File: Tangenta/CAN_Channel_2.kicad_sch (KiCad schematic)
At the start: 0 parts

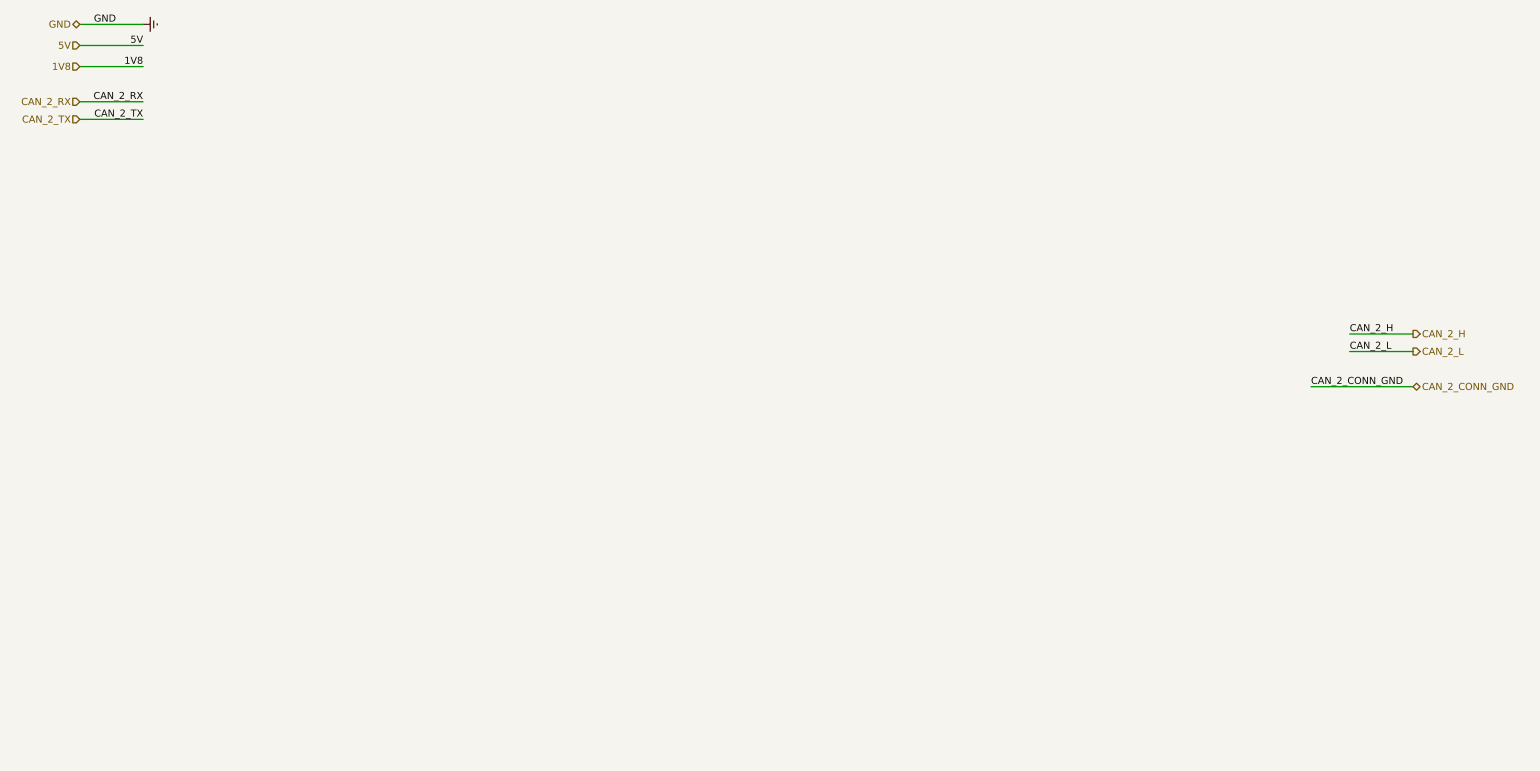
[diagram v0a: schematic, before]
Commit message: CANbus ICs schematic done.
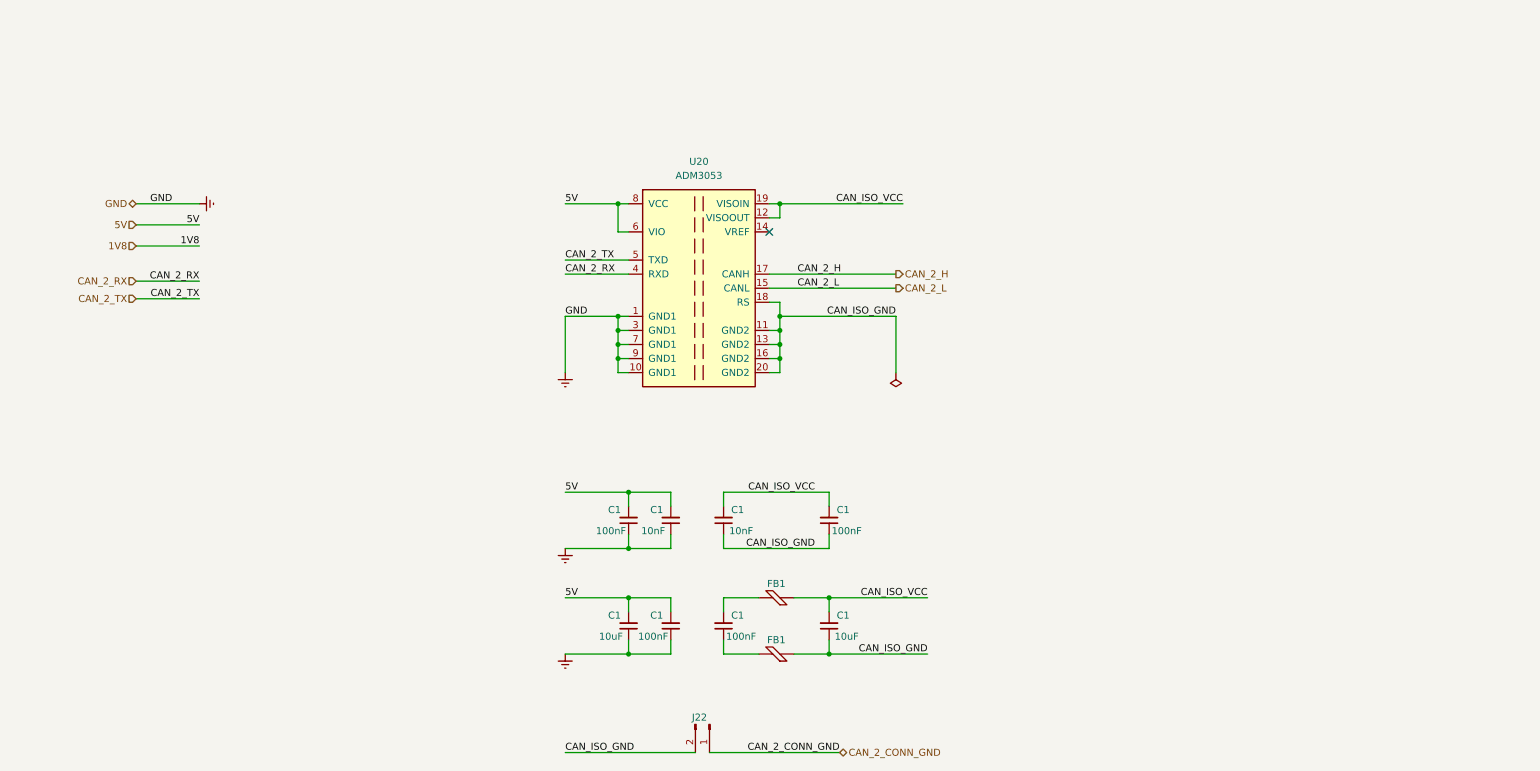
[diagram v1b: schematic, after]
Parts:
- added C1 (x4): 100nF, Capacitor_SMD:C_0402_1005Metric, symbol Device:C_Small
- added C1 (x2): 10uF, Capacitor_SMD:C_0402_1005Metric, symbol Device:C_Small
- added C1 (x2): 10nF, Capacitor_SMD:C_0402_1005Metric, symbol Device:C_Small
- added FB1 (x2): GZ2012D101TF, Ferrite_Bead_100:Ferrite_Bead_100, symbol Ferrite_Bead_100:GZ2012D101TF
- added J22: Conn_01x02_Pin, Connector_PinHeader_2.54mm:PinHeader_1x02_P2.54mm_Vertical, symbol Connector:Conn_01x02_Pin
- added U20: ADM3053, Package_SO:SOIC-20W_7.5x12.8mm_P1.27mm, symbol Interface_CAN_LIN:ADM3053
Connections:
- net 5V: now also C1.2, C1.2, C1.2, C1.2, U20.6 (VIO), U20.8 (VCC)
- net CAN_2_CONN_GND: now also J22.1 (Pin_1)
- net CAN_2_H: now also U20.17 (CANH)
- net CAN_2_L: now also U20.15 (CANL)
- net CAN_2_RX: now also U20.4 (RXD)
- net CAN_2_TX: now also U20.5 (TXD)
- net GNDREF: now also C1.1, C1.1, C1.1, C1.1, U20.1 (GND1), U20.10 (GND1), U20.3 (GND1), U20.7 (GND1), U20.9 (GND1)
- new net: C1.1, FB1.1
- new net: C1.2, FB1.1
- new net CAN_ISO_GND: C1.1, C1.1, C1.1, FB1.2, J22.2 (Pin_2), U20.11 (GND2), U20.13 (GND2), U20.16 (GND2), U20.18 (RS), U20.20 (GND2)
- new net CAN_ISO_VCC: C1.2, C1.2, C1.2, FB1.2, U20.12 (VISOOUT), U20.19 (VISOIN)
- no-connect marks 0 -> 1

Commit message: CANbus - current progress.
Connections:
- net CAN_ISO_GND: now also C1.1, FB1.1; no longer C1.1, FB1.2
- net CAN_ISO_VCC: now also C1.2, FB1.1; no longer C1.2, FB1.2
- new net: C1.2, FB1.2
- new net: C1.1, FB1.2
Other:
- moved on the sheet: C1, FB1
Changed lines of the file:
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@@
   (junction (at 151.765 80.01) (diameter 0) (color 0 0 0 0)
   )
-  (junction (at 160.655 140.97) (diameter 0) (color 0 0 0 0)
+  (junction (at 159.385 130.81) (diameter 0) (color 0 0 0 0)
   )
   (junction (at 124.46 121.92) (diameter 0) (color 0 0 0 0)
@@
   (junction (at 151.765 59.69) (diameter 0) (color 0 0 0 0)
   )
+  (junction (at 159.385 140.97) (diameter 0) (color 0 0 0 0)
+  )
   (junction (at 151.765 85.09) (diameter 0) (color 0 0 0 0)
   )
@@
   )
   (junction (at 122.555 85.09) (diameter 0) (color 0 0 0 0)
-  )
-  (junction (at 160.655 130.81) (diameter 0) (color 0 0 0 0)
   )
   (junction (at 122.555 80.01) (diameter 0) (color 0 0 0 0)
@@
     (stroke (width 0) (type default))
   )
-  (wire (pts (xy 160.655 140.97) (xy 178.435 140.97))
+  (wire (pts (xy 159.385 140.97) (xy 141.605 140.97))
     (stroke (width 0) (type default))
   )
@@
     (stroke (width 0) (type default))
   )
-  (wire (pts (xy 160.655 130.81) (xy 160.655 133.35))
+  (wire (pts (xy 178.435 130.81) (xy 178.435 133.35))
     (stroke (width 0) (type default))
   )
@@
     (stroke (width 0) (type default))
   )
-  (wire (pts (xy 160.655 138.43) (xy 160.655 140.97))
+  (wire (pts (xy 178.435 138.43) (xy 178.435 140.97))
     (stroke (width 0) (type default))
   )
@@
     (stroke (width 0) (type default))
   )
-  (wire (pts (xy 154.305 140.97) (xy 160.655 140.97))
+  (wire (pts (xy 172.085 140.97) (xy 178.435 140.97))
     (stroke (width 0) (type default))
   )
@@
     (stroke (width 0) (type default))
   )
-  (wire (pts (xy 154.305 130.81) (xy 160.655 130.81))
+  (wire (pts (xy 172.085 130.81) (xy 178.435 130.81))
     (stroke (width 0) (type default))
   )
@@
     (stroke (width 0) (type default))
   )
-  (wire (pts (xy 160.655 130.81) (xy 178.435 130.81))
+  (wire (pts (xy 159.385 130.81) (xy 141.605 130.81))
     (stroke (width 0) (type default))
   )
@@
     (stroke (width 0) (type default))
   )
-  (wire (pts (xy 141.605 130.81) (xy 141.605 133.35))
+  (wire (pts (xy 159.385 130.81) (xy 159.385 133.35))
     (stroke (width 0) (type default))
   )
@@
     (stroke (width 0) (type default))
   )
-  (wire (pts (xy 141.605 130.81) (xy 147.955 130.81))
+  (wire (pts (xy 159.385 130.81) (xy 165.735 130.81))
     (stroke (width 0) (type default))
   )
@@
     (stroke (width 0) (type default))
   )
-  (wire (pts (xy 141.605 140.97) (xy 147.955 140.97))
+  (wire (pts (xy 159.385 140.97) (xy 165.735 140.97))
     (stroke (width 0) (type default))
   )
@@
     (stroke (width 0) (type default))
   )
-  (wire (pts (xy 141.605 138.43) (xy 141.605 140.97))
+  (wire (pts (xy 159.385 138.43) (xy 159.385 140.97))
     (stroke (width 0) (type default))
   )
@@
     (effects (font (size 1.27 1.27)) (justify left bottom))
   )
-  (label "CAN_ISO_VCC" (at 178.435 130.81 180) (fields_autoplaced)
-    (effects (font (size 1.27 1.27)) (justify right bottom))
+  (label "CAN_ISO_VCC" (at 141.605 130.81 0) (fields_autoplaced)
+    (effects (font (size 1.27 1.27)) (justify left bottom))
   )
   (label "CAN_2_TX" (at 113.03 69.85 0) (fields_autoplaced)
@@
     (effects (font (size 1.27 1.27)) (justify right bottom))
   )
-  (label "CAN_ISO_GND" (at 178.435 140.97 180) (fields_autoplaced)
-    (effects (font (size 1.27 1.27)) (justify right bottom))
+  (label "CAN_ISO_GND" (at 141.605 140.97 0) (fields_autoplaced)
+    (effects (font (size 1.27 1.27)) (justify left bottom))
   )
   (label "CAN_ISO_GND" (at 158.115 121.92 180) (fields_autoplaced)
@@
     )
   )
-  (symbol (lib_id "Device:C_Small") (at 141.605 135.89 0) (mirror x) (unit 1)
-    (in_bom yes) (on_board yes) (dnp no)
-    (property "Reference" "C1" (at 144.1451 133.9849 0)
-      (effects (font (size 1.27 1.27)))
-    )
-    (property "Value" "100nF" (at 144.78 137.795 0)
-      (effects (font (size 1.27 1.27)))
-    )
-    (property "Footprint" "Capacitor_SMD:C_0402_1005Metric" (at 141.605 135.89 0)
-      (effects (font (size 1.27 1.27)) hide)
-    )
-    (property "Datasheet" "~" (at 141.605 135.89 0)
+  (symbol (lib_id "Device:C_Small") (at 159.385 135.89 0) (mirror x) (unit 1)
+    (in_bom yes) (on_board yes) (dnp no)
+    (property "Reference" "C1" (at 161.9251 133.9849 0)
+      (effects (font (size 1.27 1.27)))
+    )
+    (property "Value" "100nF" (at 162.56 137.795 0)
+      (effects (font (size 1.27 1.27)))
+    )
+    (property "Footprint" "Capacitor_SMD:C_0402_1005Metric" (at 159.385 135.89 0)
+      (effects (font (size 1.27 1.27)) hide)
+    )
+    (property "Datasheet" "~" (at 159.385 135.89 0)
       (effects (font (size 1.27 1.27)) hide)
     )
@@
     )
   )
-  (symbol (lib_id "Ferrite_Bead_100:GZ2012D101TF") (at 151.13 130.81 0) (unit 1)
-    (in_bom yes) (on_board yes) (dnp no)
-    (property "Reference" "FB1" (at 151.13 128.27 0)
-      (effects (font (size 1.27 1.27)))
-    )
-    (property "Value" "GZ2012D101TF" (at 151.13 127 0)
-      (effects (font (size 1.27 1.27)) hide)
-    )
-    (property "Footprint" "Ferrite_Bead_100:Ferrite_Bead_100" (at 163.703 140.843 0)
+  (symbol (lib_id "Ferrite_Bead_100:GZ2012D101TF") (at 168.91 130.81 0) (unit 1)
+    (in_bom yes) (on_board yes) (dnp no)
+    (property "Reference" "FB1" (at 168.91 128.27 0)
+      (effects (font (size 1.27 1.27)))
+    )
+    (property "Value" "GZ2012D101TF" (at 168.91 127 0)
+      (effects (font (size 1.27 1.27)) hide)
+    )
+    (property "Footprint" "Ferrite_Bead_100:Ferrite_Bead_100" (at 181.483 140.843 0)
       (effects (font (size 1.27 1.27) italic) hide)
     )
-    (property "Datasheet" "https://item.szlcsc.com/344132.html" (at 146.939 138.557 0)
+    (property "Datasheet" "https://item.szlcsc.com/344132.html" (at 164.719 138.557 0)
       (effects (font (size 1.27 1.27)) (justify left) hide)
     )
-    (property "LCSC" "C1015" (at 149.987 134.239 0)
+    (property "LCSC" "C1015" (at 167.767 134.239 0)
       (effects (font (size 1.27 1.27)) hide)
     )
@@
     )
   )
-  (symbol (lib_id "Ferrite_Bead_100:GZ2012D101TF") (at 151.13 140.97 0) (unit 1)
-    (in_bom yes) (on_board yes) (dnp no)
-    (property "Reference" "FB1" (at 151.13 138.43 0)
-      (effects (font (size 1.27 1.27)))
-    )
-    (property "Value" "GZ2012D101TF" (at 151.13 137.16 0)
-      (effects (font (size 1.27 1.27)) hide)
-    )
-    (property "Footprint" "Ferrite_Bead_100:Ferrite_Bead_100" (at 163.703 151.003 0)
+  (symbol (lib_id "Ferrite_Bead_100:GZ2012D101TF") (at 168.91 140.97 0) (unit 1)
+    (in_bom yes) (on_board yes) (dnp no)
+    (property "Reference" "FB1" (at 168.91 138.43 0)
+      (effects (font (size 1.27 1.27)))
+    )
+    (property "Value" "GZ2012D101TF" (at 168.91 137.16 0)
+      (effects (font (size 1.27 1.27)) hide)
+    )
+    (property "Footprint" "Ferrite_Bead_100:Ferrite_Bead_100" (at 181.483 151.003 0)
       (effects (font (size 1.27 1.27) italic) hide)
     )
-    (property "Datasheet" "https://item.szlcsc.com/344132.html" (at 146.939 148.717 0)
+    (property "Datasheet" "https://item.szlcsc.com/344132.html" (at 164.719 148.717 0)
       (effects (font (size 1.27 1.27)) (justify left) hide)
     )
-    (property "LCSC" "C1015" (at 149.987 144.399 0)
+    (property "LCSC" "C1015" (at 167.767 144.399 0)
       (effects (font (size 1.27 1.27)) hide)
     )
@@
     )
   )
-  (symbol (lib_id "Device:C_Small") (at 160.655 135.89 0) (mirror x) (unit 1)
-    (in_bom yes) (on_board yes) (dnp no)
-    (property "Reference" "C1" (at 163.1951 133.9849 0)
-      (effects (font (size 1.27 1.27)))
-    )
-    (property "Value" "10uF" (at 163.83 137.795 0)
-      (effects (font (size 1.27 1.27)))
-    )
-    (property "Footprint" "Capacitor_SMD:C_0402_1005Metric" (at 160.655 135.89 0)
-      (effects (font (size 1.27 1.27)) hide)
-    )
-    (property "Datasheet" "~" (at 160.655 135.89 0)
-      (effects (font (size 1.27 1.27)) hide)
-    )
+  (symbol (lib_id "Device:C_Small") (at 178.435 135.89 0) (mirror x) (unit 1)
+    (in_bom yes) (on_board yes) (dnp no)
+    (property "Reference" "C1" (at 180.9751 133.9849 0)
+      (effects (font (size 1.27 1.27)))
+    )
+    (property "Value" "10uF" (at 181.61 137.795 0)
+      (effects (font (size 1.27 1.27)))
+    )
+    (property "Footprint" "Capacitor_SMD:C_0402_1005Metric" (at 178.435 135.89 0)
+      (effects (font (size 1.27 1.27)) hide)
+    )
+    (property "Datasheet" "~" (at 178.435 135.89 0)
+      (effects (font (size 1.27 1.27)) hide)
+    )

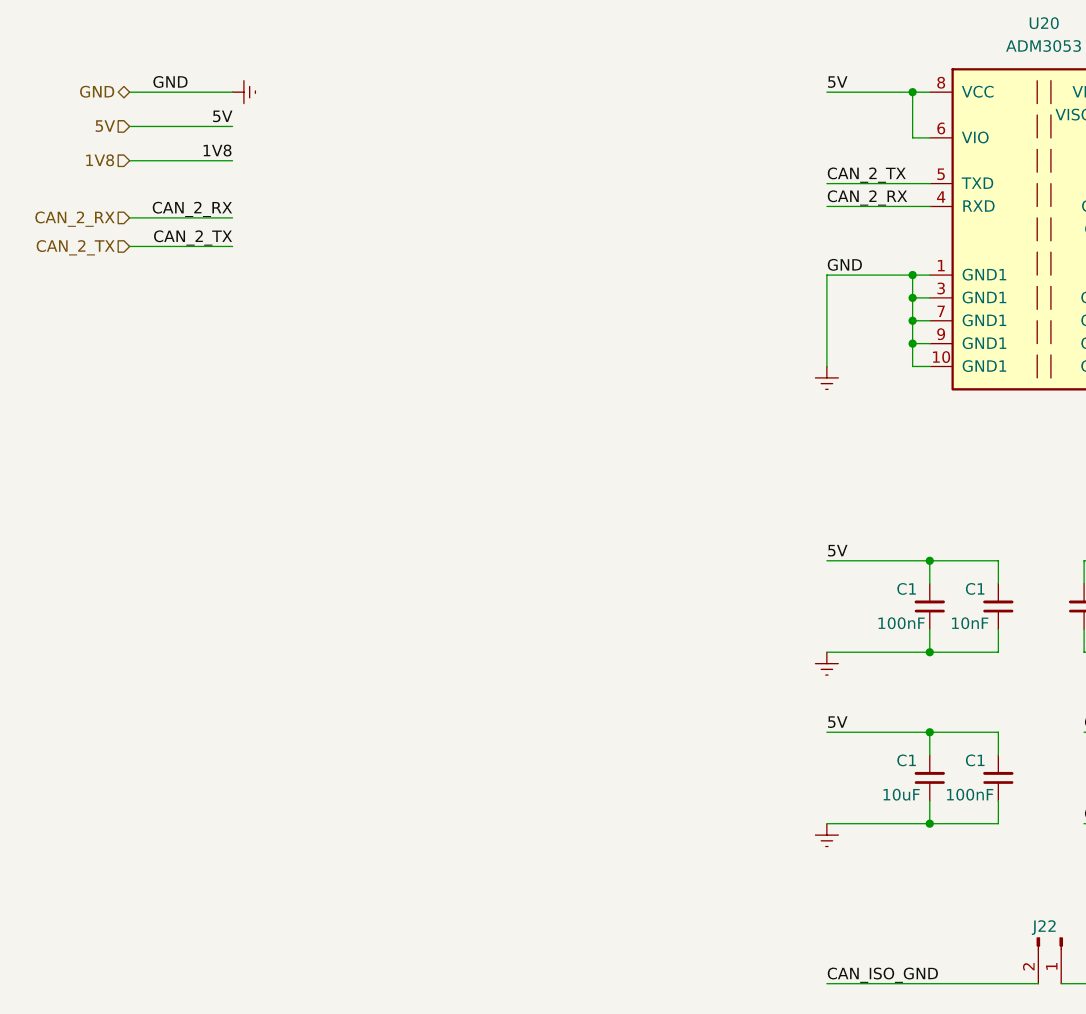
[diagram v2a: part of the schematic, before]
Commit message: CANbus current progress, RS-422 with 0603 termination resistor.
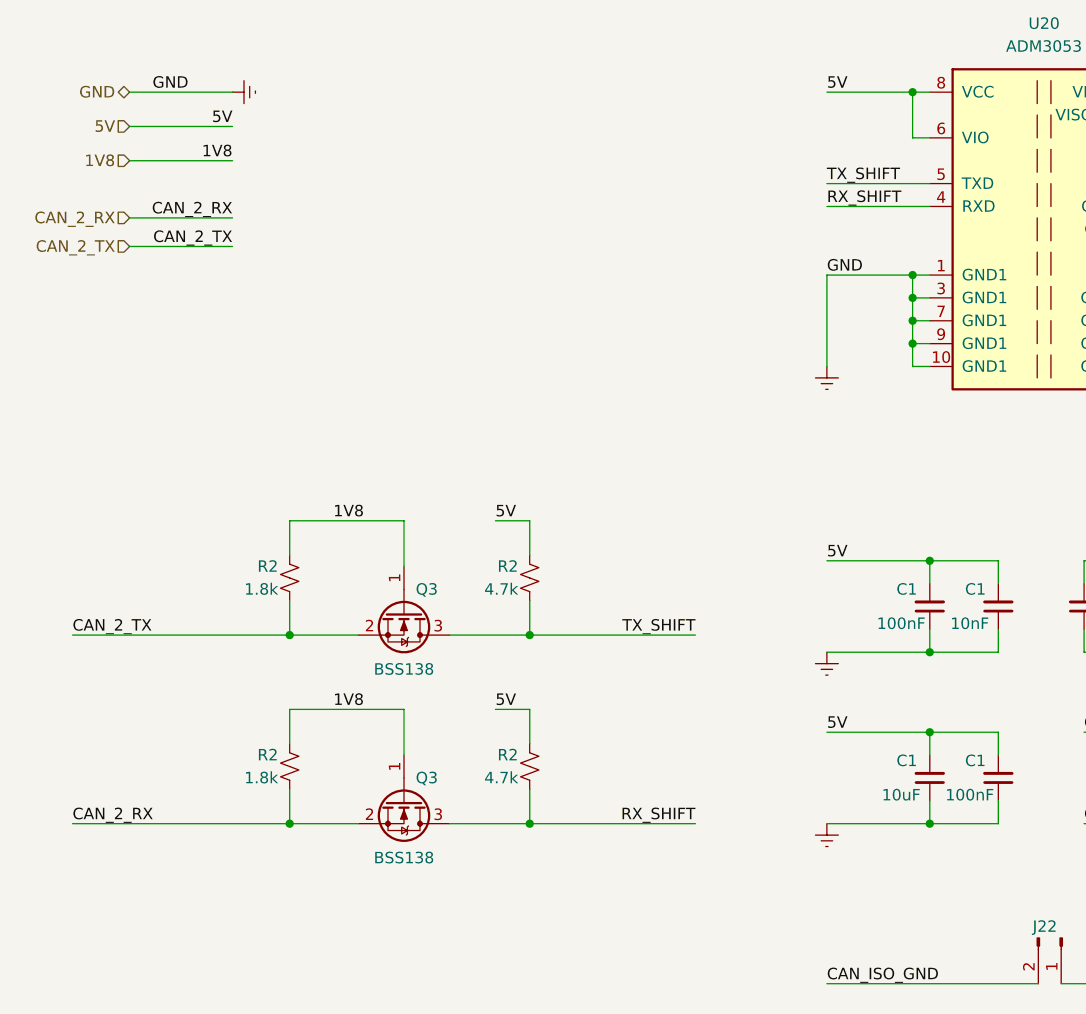
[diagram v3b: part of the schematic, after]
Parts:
- added Q3 (x2): BSS138, Package_TO_SOT_SMD:SOT-23, symbol Transistor_FET:BSS138
- added R2 (x2): 4.7k, Resistor_SMD:R_0402_1005Metric, symbol Device:R_Small_US
- added R2 (x2): 1.8k, Resistor_SMD:R_0402_1005Metric, symbol Device:R_Small_US
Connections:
- net 1V8: now also Q3.1 (G), Q3.1 (G), R2.2, R2.2
- net 5V: now also R2.2, R2.2
- net CAN_2_RX: now also Q3.2 (S), R2.1; no longer U20.4 (RXD)
- net CAN_2_TX: now also Q3.2 (S), R2.1; no longer U20.5 (TXD)
- new net RX_SHIFT: Q3.3 (D), R2.1, U20.4 (RXD)
- new net TX_SHIFT: Q3.3 (D), R2.1, U20.5 (TXD)
